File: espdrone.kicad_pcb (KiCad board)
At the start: 6 copper layers, 55 x 55 mm, 565 parts, among them J1 Conn_02x03_Odd_Even, J10 Conn_01x04_Pin, J12 Conn_01x14, J2 Conn_01x02, J3 Conn_Coaxial, J4 Conn_01x04_Pin, J5 Conn_01x04, J6 Conn_01x06, J7 Conn_01x04_Pin, J8 Conn_01x04_Pin, J9 Conn_01x04_Pin, Q1 NMOS, Q10 PSMN1R4-40YLDX, Q11 PSMN1R4-40YLDX, Q12 PSMN1R4-40YLDX, Q13 PSMN1R4-40YLDX, Q14 PSMN1R4-40YLDX, Q15 PSMN1R4-40YLDX, Q16 PSMN1R4-40YLDX, Q17 PSMN1R4-40YLDX, Q18 PSMN1R4-40YLDX, Q19 PSMN1R4-40YLDX, Q2 NMOS, Q20 PSMN1R4-40YLDX, Q21 PSMN1R4-40YLDX, Q22 PSMN1R4-40YLDX, Q23 PSMN1R4-40YLDX, Q24 PSMN1R4-40YLDX, Q25 PSMN1R4-40YLDX, Q26 PSMN1R4-40YLDX, Q27 PSMN1R4-40YLDX, Q28 PSMN1R4-40YLDX, Q3 NMOS, Q4 NMOS, Q5 PSMN1R4-40YLDX, Q6 PSMN1R4-40YLDX, Q7 PSMN1R4-40YLDX, Q8 PSMN1R4-40YLDX, Q9 PSMN1R4-40YLDX, U10 INA180A2, U11 FPC-1.0FX-15PWCR-H20, U12 VL53L1CXV0FY1, U13 LIS2MDL, U14 LSM6DS3, U15 PMW3901MB-TXQT_C43496881, U16 STM32G071K8U6, U17 DRV8328ARUYR, U18 INA180A2, U19 STM32G071K8U6, U2 USBLC6-2P6, U20 DRV8328ARUYR, U21 INA180A2, U22 STM32G071K8U6, U23 DRV8328ARUYR, U24 INA180A2, U25 STM32G071K8U6, U26 DRV8328ARUYR, U27 INA180A2, U3 W25Q128JVP, U4 LFD182G45DCHD277, U5 ESP32-C5HF4, U6 TLV62569DBV, U7 XC6206P182MR_C347373, U8 TPS63070RNMR, U9 TPS2121RUXR, Y1 Crystal_GND24, Y2 Crystal_GND24

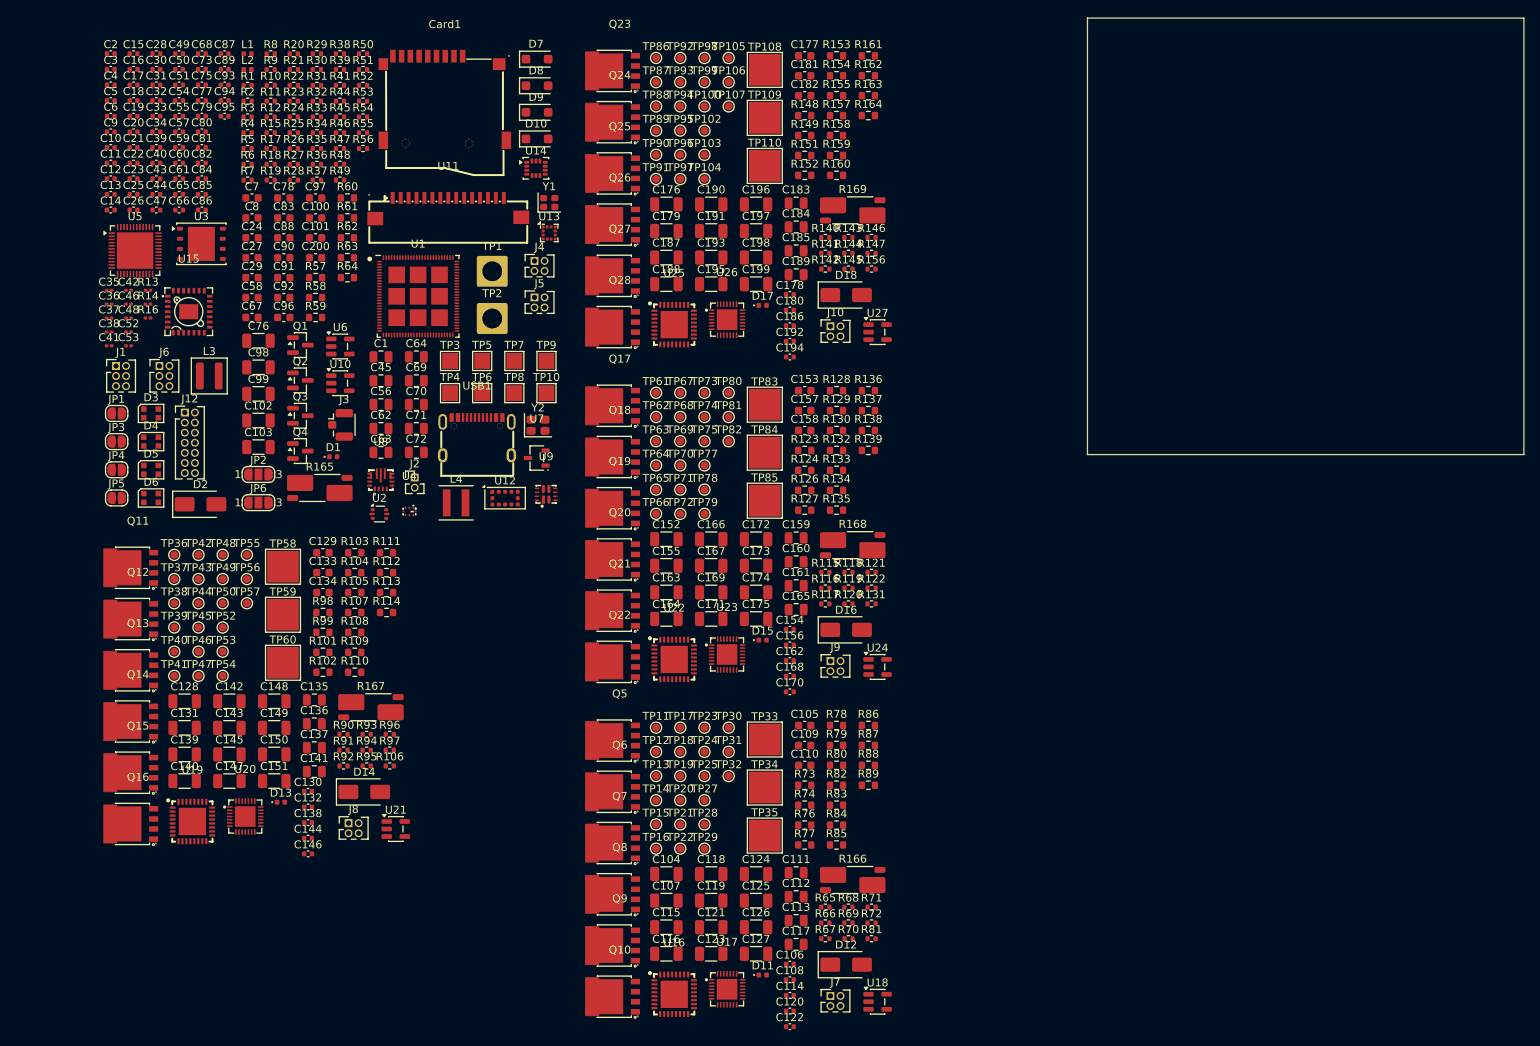
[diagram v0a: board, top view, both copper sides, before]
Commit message: Remove a lot of test points
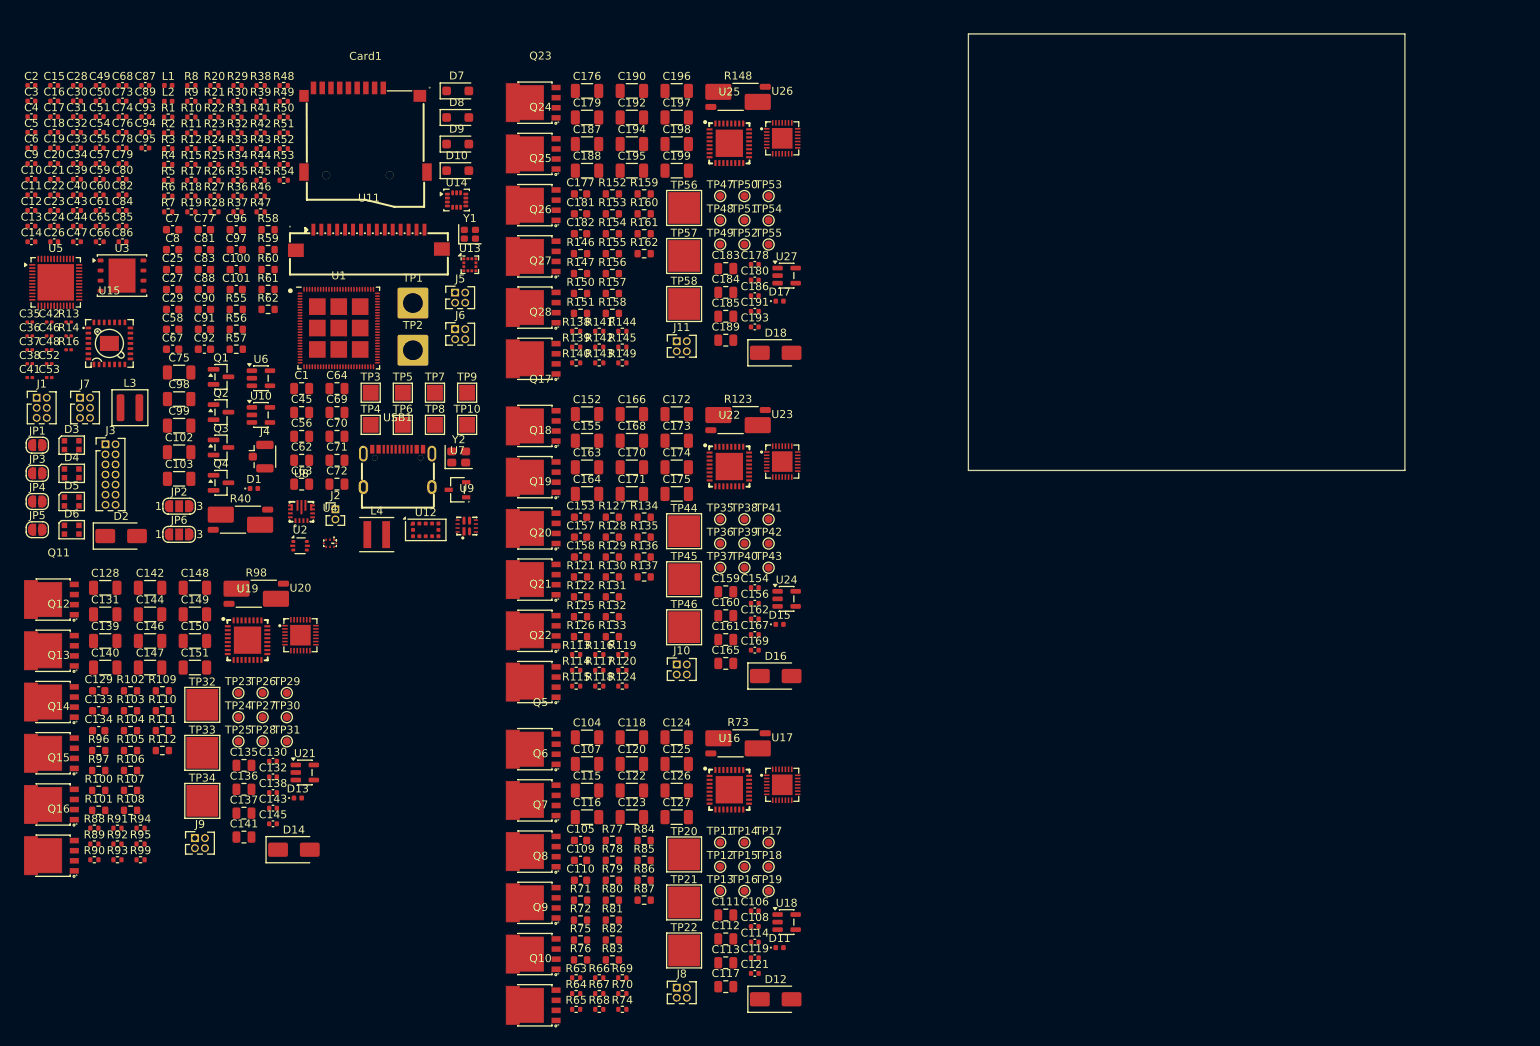
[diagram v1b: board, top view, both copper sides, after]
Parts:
- removed C200: 1u, Capacitor_SMD:C_0603_1608Metric
- removed J12: Conn_01x14, Connector_PinHeader_1.27mm:PinHeader_2x07_P1.27mm_Vertical
- removed R163: 1k, Resistor_SMD:R_0603_1608Metric
- removed R164: 10k, Resistor_SMD:R_0603_1608Metric
- removed R165: 0.0005, Resistor_SMD:R_Shunt_Vishay_WSK2512_6332Metric_T2.66mm
- removed R166, R167, R168, R169: 0.001, Resistor_SMD:R_Shunt_Vishay_WSK2512_6332Metric_T2.66mm
- removed TP100, TP102, TP103, TP104, TP105, TP106, TP107, TP61, TP62, TP63, TP64, TP65, TP66, TP67, TP68, TP69, TP70, TP71, TP72, TP73, TP74, TP75, TP77, TP78, TP79, TP80, TP81, TP82, TP86, TP87, TP88, TP89, TP90, TP91, TP92, TP93, TP94, TP95, TP96, TP97, TP98, TP99: TestPoint, TestPoint:TestPoint_Pad_D1.0mm
- removed TP108, TP83: MOT_A, TestPoint:TestPoint_Pad_4.0x4.0mm
- removed TP109, TP59, TP84: MOT_B, TestPoint:TestPoint_Pad_4.0x4.0mm
- removed TP110, TP60, TP85: MOT_C, TestPoint:TestPoint_Pad_4.0x4.0mm
- added C74: 1n, Capacitor_SMD:C_0402_1005Metric, F.Cu at (65.4, 44.4)
- added J11: Conn_01x04_Pin, Connector_PinHeader_1.27mm:PinHeader_2x02_P1.27mm_Vertical, F.Cu at (135.2, 72.7)
- added R100: 10k, Resistor_SMD:R_0603_1608Metric, F.Cu at (62.4, 129.3)
- added R125: 10k, Resistor_SMD:R_0603_1608Metric, F.Cu at (123.1, 107.4)
- added R150: 10k, Resistor_SMD:R_0603_1608Metric, F.Cu at (123.1, 66.7)
- added R40: 0.0005, Resistor_SMD:R_Shunt_Vishay_WSK2512_6332Metric_T2.66mm, F.Cu at (80.3, 95.2)
- added R42: 47k, Resistor_SMD:R_0402_1005Metric, F.Cu at (82.8, 46.5)
- added R43: 47k, Resistor_SMD:R_0402_1005Metric, F.Cu at (82.8, 48.5)
- added R75: 10k, Resistor_SMD:R_0603_1608Metric, F.Cu at (123.1, 148.2)
- added TP26: TestPoint, TestPoint:TestPoint_Pad_D1.0mm, F.Cu at (83.1, 117.0)
- added TP51: TestPoint, TestPoint:TestPoint_Pad_D1.0mm, F.Cu at (143.8, 57.5)
- C119, C143, C167, C191: value 10u -> 100n; footprint Capacitor_SMD:C_1206_3216Metric -> Capacitor_SMD:C_0402_1005Metric
- C120, C144, C168, C192: value 100n -> 10u; footprint Capacitor_SMD:C_0402_1005Metric -> Capacitor_SMD:C_1206_3216Metric
- C121, C145, C169, C193: value 10u -> 1n; footprint Capacitor_SMD:C_1206_3216Metric -> Capacitor_SMD:C_0402_1005Metric
- C122, C146, C170, C194: value 1n -> 10u; footprint Capacitor_SMD:C_0402_1005Metric -> Capacitor_SMD:C_1206_3216Metric
- C24: value 4.7u -> 100n; footprint Capacitor_SMD:C_0603_1608Metric -> Capacitor_SMD:C_0402_1005Metric
- C25: value 100n -> 4.7u; footprint Capacitor_SMD:C_0402_1005Metric -> Capacitor_SMD:C_0603_1608Metric
- C75: value 1n -> 100u; footprint Capacitor_SMD:C_0402_1005Metric -> Capacitor_SMD:C_1206_3216Metric
- C76: value 100u -> 100n; footprint Capacitor_SMD:C_1206_3216Metric -> Capacitor_SMD:C_0402_1005Metric
- C77: value 100n -> 10u; footprint Capacitor_SMD:C_0402_1005Metric -> Capacitor_SMD:C_0603_1608Metric
- C78: value 10u -> 100n; footprint Capacitor_SMD:C_0603_1608Metric -> Capacitor_SMD:C_0402_1005Metric
- C81: value 100n -> 1u; footprint Capacitor_SMD:C_0402_1005Metric -> Capacitor_SMD:C_0603_1608Metric
- J3: value Conn_Coaxial -> Conn_01x14; footprint Connector_Coaxial:U.FL_Hirose_U.FL-R-SMT-1_Vertical -> Connector_PinHeader_1.27mm:PinHeader_2x07_P1.27mm_Vertical
- J4: value Conn_01x04_Pin -> Conn_Coaxial; footprint Connector_PinHeader_1.27mm:PinHeader_2x02_P1.27mm_Vertical -> Connector_Coaxial:U.FL_Hirose_U.FL-R-SMT-1_Vertical
- J5: value Conn_01x04 -> Conn_01x04_Pin
- J6: value Conn_01x06 -> Conn_01x04; footprint Connector_PinHeader_1.27mm:PinHeader_2x03_P1.27mm_Vertical -> Connector_PinHeader_1.27mm:PinHeader_2x02_P1.27mm_Vertical
- J7: value Conn_01x04_Pin -> Conn_01x06; footprint Connector_PinHeader_1.27mm:PinHeader_2x02_P1.27mm_Vertical -> Connector_PinHeader_1.27mm:PinHeader_2x03_P1.27mm_Vertical
- R101, R120, R126, R145, R151, R70, R76, R95: value 10k -> 1k
- R102, R108, R127, R133, R152, R158, R77, R83: value 1k -> 10
- R104, R110, R129, R135, R154, R160, R57, R58, R61, R62, R79, R85: value 10 -> 10k
- R106, R131, R156, R81: footprint Resistor_SMD:R_0402_1005Metric -> Resistor_SMD:R_0603_1608Metric
- R109, R134, R159, R59, R60, R84: value 10k -> 10
- R111, R136, R161, R86: value 10 -> 1k
- R113, R138, R88: value 1k -> 4.7k; footprint Resistor_SMD:R_0603_1608Metric -> Resistor_SMD:R_0402_1005Metric
- R114, R139, R63, R64, R89: value 10k -> 4.7k; footprint Resistor_SMD:R_0603_1608Metric -> Resistor_SMD:R_0402_1005Metric
- R115, R140, R65, R90: value 4.7k -> 10k
- R116, R141, R66, R91: value 4.7k -> 1k
- R117, R142, R67, R92: value 10k -> 220k
- R118, R143, R68, R93: value 1k -> 10k
- R119, R144, R69, R94: value 220k -> 10k
- R121, R146, R55, R71, R96: value 10k -> 10; footprint Resistor_SMD:R_0402_1005Metric -> Resistor_SMD:R_0603_1608Metric
- R122, R147, R72, R97: value 1k -> 10; footprint Resistor_SMD:R_0402_1005Metric -> Resistor_SMD:R_0603_1608Metric
- R123, R148, R73, R98: value 10 -> 0.001; footprint Resistor_SMD:R_0603_1608Metric -> Resistor_SMD:R_Shunt_Vishay_WSK2512_6332Metric_T2.66mm
- R124, R149, R74, R99: value 10 -> 1k; footprint Resistor_SMD:R_0603_1608Metric -> Resistor_SMD:R_0402_1005Metric
- R34: value 100k -> 10k
- R35: value 10k -> 5k
- R36: value 5k -> 100k
- R47, R48: value 47k -> 10k
- R54: value 10k -> 4.7k
- R56: value 4.7k -> 10; footprint Resistor_SMD:R_0402_1005Metric -> Resistor_SMD:R_0603_1608Metric
- TP20, TP32, TP44, TP56: value TestPoint -> MOT_A; footprint TestPoint:TestPoint_Pad_D1.0mm -> TestPoint:TestPoint_Pad_4.0x4.0mm
- TP21, TP45, TP57: value TestPoint -> MOT_B; footprint TestPoint:TestPoint_Pad_D1.0mm -> TestPoint:TestPoint_Pad_4.0x4.0mm
- TP22, TP46: value TestPoint -> MOT_C; footprint TestPoint:TestPoint_Pad_D1.0mm -> TestPoint:TestPoint_Pad_4.0x4.0mm
- TP33: value MOT_A -> MOT_B
- TP34: value MOT_B -> MOT_C
- TP35: value MOT_C -> TestPoint; footprint TestPoint:TestPoint_Pad_4.0x4.0mm -> TestPoint:TestPoint_Pad_D1.0mm
- TP58: value MOT_A -> MOT_C
- moved J7 120.9 mm to (60.1, 79.8)
- moved R88 97.9 mm to (61.9, 134.1)
- moved R89 97.8 mm to (61.9, 136.1)
- moved R63 95.2 mm to (122.6, 152.9)
- moved R64 94.7 mm to (122.6, 154.9)
- moved TP53 89.6 mm to (146.8, 54.4)
- moved TP54 89.6 mm to (146.8, 57.5)
- moved TP47 89.3 mm to (140.7, 54.4)
- moved TP50 83.4 mm to (143.8, 54.4)
- moved J9 83.1 mm to (74.5, 135.3)
- moved TP52 81.6 mm to (143.8, 60.5)
- moved TP41 77.4 mm to (146.8, 95.2)
- moved TP55 76.5 mm to (146.8, 60.5)
- moved TP48 75.5 mm to (140.7, 57.5)
- moved TP49 75.5 mm to (140.7, 60.5)
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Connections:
- C119 pad 1: GND -> +3V3
- C119 pad 2: +BATT -> GND
- C120 pad 1: +3V3 -> GND
- C120 pad 2: GND -> +BATT
- C121 pad 1: GND -> /Motors/ESC/ISENSE
- C121 pad 2: +BATT -> GND
- C122 pad 1: /Motors/ESC/ISENSE -> GND
- C122 pad 2: GND -> +BATT
- C143 pad 1: GND -> +3V3
- C143 pad 2: +BATT -> GND
- C144 pad 1: +3V3 -> GND
- C144 pad 2: GND -> +BATT
- C145 pad 1: GND -> /Motors/ESC1/ISENSE
- C145 pad 2: +BATT -> GND
- C146 pad 1: /Motors/ESC1/ISENSE -> GND
- C146 pad 2: GND -> +BATT
- C167 pad 1: GND -> +3V3
- C167 pad 2: +BATT -> GND
- C168 pad 1: +3V3 -> GND
- C168 pad 2: GND -> +BATT
- C169 pad 1: GND -> /Motors/ESC2/ISENSE
- C169 pad 2: +BATT -> GND
- C170 pad 1: /Motors/ESC2/ISENSE -> GND
- C170 pad 2: GND -> +BATT
- C191 pad 1: GND -> +3V3
- C191 pad 2: +BATT -> GND
- C192 pad 1: +3V3 -> GND
- C192 pad 2: GND -> +BATT
- C193 pad 1: GND -> /Motors/ESC3/ISENSE
- C193 pad 2: +BATT -> GND
- C194 pad 1: /Motors/ESC3/ISENSE -> GND
- C194 pad 2: GND -> +BATT
- C20 pad 1: +3V3 -> VDD_HP
- C21 pad 1: VDD_HP -> +3V3
- C23 pad 1: VDD_HP -> +3V3
- C24 pad 1: +3V3 -> VDD_HP
- C42 pad 1: Net-(J3-In) -> Net-(J4-In)
- C75 pad 1: BAT_ISENSE -> GND
- C75 pad 2: GND -> Net-(C75-Pad2)
- C76 pad 2: Net-(C76-Pad2) -> +3V3
- C78 pad 1: GND -> +3V3
- C78 pad 2: +3V3 -> GND
- C81 pad 1: +3V3 -> GND
- C81 pad 2: GND -> +3V3
- J10 pad 2: /Motors/ESC3/SWDIO -> /Motors/ESC2/SWDIO
- J10 pad 3: /Motors/ESC3/SWCLK -> /Motors/ESC2/SWCLK
- J3 pad 1: Net-(J3-In) -> +3V3
- J3 pad 2: GND -> /MCU/GPIO6
- J4 pad 1: Net-(J4-Pin_1) -> Net-(J4-In)
- J4 pad 2: Net-(J4-Pin_2) -> GND
- J5 pad 1: +3V3 -> Net-(J5-Pin_1)
- J5 pad 2: I2C_SDA -> Net-(J5-Pin_2)
- J5 pad 3: I2C_SCL -> Net-(J5-Pin_3)
- J5 pad 4: GND -> Net-(J5-Pin_4)
- J6 pad 2: SPI_CLK -> I2C_SDA
- J6 pad 3: SPI_EXT_CS -> I2C_SCL
- J6 pad 4: SPI_MISO -> GND
- J7 pad 2: /Motors/ESC/SWDIO -> SPI_CLK
- J7 pad 3: /Motors/ESC/SWCLK -> SPI_EXT_CS
- J7 pad 4: GND -> SPI_MISO
- J8 pad 2: /Motors/ESC1/SWDIO -> /Motors/ESC/SWDIO
- J8 pad 3: /Motors/ESC1/SWCLK -> /Motors/ESC/SWCLK
- J9 pad 2: /Motors/ESC2/SWDIO -> /Motors/ESC1/SWDIO
- J9 pad 3: /Motors/ESC2/SWCLK -> /Motors/ESC1/SWCLK
- JP2 pad 2: Net-(J4-Pin_2) -> Net-(J5-Pin_2)
- R101 pad 1: /Motors/ESC1/VSENSE_A -> GND
- R101 pad 2: /Motors/ESC1/VSENSE_REF -> /Motors/ESC1/VSENSE_A
- R102 pad 1: GND -> Net-(Q13-G)
- R102 pad 2: /Motors/ESC1/VSENSE_A -> /Motors/ESC1/GHB
- R103 pad 1: Net-(Q13-G) -> Net-(Q14-G)
- R103 pad 2: /Motors/ESC1/GHB -> /Motors/ESC1/GLB
- R104 pad 1: Net-(Q14-G) -> /Motors/ESC1/A
- R104 pad 2: /Motors/ESC1/GLB -> /Motors/ESC1/VSENSE_A
- R105 pad 1: /Motors/ESC1/A -> /Motors/ESC1/VSENSE_B
- R105 pad 2: /Motors/ESC1/VSENSE_A -> /Motors/ESC1/VSENSE_REF
- R106 pad 1: /Motors/ESC1/ISENSE -> GND
- R106 pad 2: Net-(R106-Pad2) -> /Motors/ESC1/VSENSE_B
- R107 pad 1: /Motors/ESC1/VSENSE_B -> /Motors/ESC1/B
- R107 pad 2: /Motors/ESC1/VSENSE_REF -> /Motors/ESC1/VSENSE_B
- R108 pad 1: GND -> Net-(Q15-G)
- R108 pad 2: /Motors/ESC1/VSENSE_B -> /Motors/ESC1/GHC
- R109 pad 1: /Motors/ESC1/B -> Net-(Q16-G)
- R109 pad 2: /Motors/ESC1/VSENSE_B -> /Motors/ESC1/GLC
- R110 pad 1: Net-(Q15-G) -> /Motors/ESC1/VSENSE_C
- R110 pad 2: /Motors/ESC1/GHC -> /Motors/ESC1/VSENSE_REF
- R111 pad 1: Net-(Q16-G) -> GND
- R111 pad 2: /Motors/ESC1/GLC -> /Motors/ESC1/VSENSE_C
- R112 pad 1: /Motors/ESC1/VSENSE_C -> /Motors/ESC1/C
- R112 pad 2: /Motors/ESC1/VSENSE_REF -> /Motors/ESC1/VSENSE_C
- R113 pad 1: GND -> Net-(U22-PA0)
- R113 pad 2: /Motors/ESC1/VSENSE_C -> Net-(D15-A)
- R114 pad 1: /Motors/ESC1/C -> +3V3
- R114 pad 2: /Motors/ESC1/VSENSE_C -> /Motors/ESC2/NFAULT
- R115 pad 1: Net-(U22-PA0) -> Net-(U23-DT)
- R115 pad 2: Net-(D15-A) -> GND
- R116 pad 1: +3V3 -> Net-(U22-PB4)
- R116 pad 2: /Motors/ESC2/NFAULT -> DSHOT_3
- R117 pad 1: Net-(U23-DT) -> Net-(U23-VDSLVL)
- R117 pad 2: GND -> +3V3
- R118 pad 1: Net-(U22-PB4) -> GND
- R118 pad 2: DSHOT_3 -> Net-(U23-VDSLVL)
- R119 pad 1: Net-(U23-VDSLVL) -> /Motors/ESC2/VSENSE
- R119 pad 2: +3V3 -> +BATT
- R120 pad 2: Net-(U23-VDSLVL) -> /Motors/ESC2/VSENSE
- R121 pad 1: /Motors/ESC2/VSENSE -> Net-(Q17-G)
- R121 pad 2: +BATT -> /Motors/ESC2/GHA
- R122 pad 1: GND -> Net-(Q18-G)
- R122 pad 2: /Motors/ESC2/VSENSE -> /Motors/ESC2/GLA
- R123 pad 1: Net-(Q17-G) -> GND
- R123 pad 2: /Motors/ESC2/GHA -> Net-(U24--)
- R124 pad 1: Net-(Q18-G) -> /Motors/ESC2/ISENSE
- R124 pad 2: /Motors/ESC2/GLA -> Net-(R124-Pad2)
- R126 pad 1: /Motors/ESC2/VSENSE_A -> GND
- R126 pad 2: /Motors/ESC2/VSENSE_REF -> /Motors/ESC2/VSENSE_A
- R127 pad 1: GND -> Net-(Q19-G)
- R127 pad 2: /Motors/ESC2/VSENSE_A -> /Motors/ESC2/GHB
- R128 pad 1: Net-(Q19-G) -> Net-(Q20-G)
- R128 pad 2: /Motors/ESC2/GHB -> /Motors/ESC2/GLB
- R129 pad 1: Net-(Q20-G) -> /Motors/ESC2/A
- R129 pad 2: /Motors/ESC2/GLB -> /Motors/ESC2/VSENSE_A
- R130 pad 1: /Motors/ESC2/A -> /Motors/ESC2/VSENSE_B
- R130 pad 2: /Motors/ESC2/VSENSE_A -> /Motors/ESC2/VSENSE_REF
- R131 pad 1: /Motors/ESC2/ISENSE -> GND
- R131 pad 2: Net-(R131-Pad2) -> /Motors/ESC2/VSENSE_B
- R132 pad 1: /Motors/ESC2/VSENSE_B -> /Motors/ESC2/B
- R132 pad 2: /Motors/ESC2/VSENSE_REF -> /Motors/ESC2/VSENSE_B
- R133 pad 1: GND -> Net-(Q21-G)
- R133 pad 2: /Motors/ESC2/VSENSE_B -> /Motors/ESC2/GHC
- R134 pad 1: /Motors/ESC2/B -> Net-(Q22-G)
- R134 pad 2: /Motors/ESC2/VSENSE_B -> /Motors/ESC2/GLC
- R135 pad 1: Net-(Q21-G) -> /Motors/ESC2/VSENSE_C
- R135 pad 2: /Motors/ESC2/GHC -> /Motors/ESC2/VSENSE_REF
- R136 pad 1: Net-(Q22-G) -> GND
- R136 pad 2: /Motors/ESC2/GLC -> /Motors/ESC2/VSENSE_C
- R137 pad 1: /Motors/ESC2/VSENSE_C -> /Motors/ESC2/C
- R137 pad 2: /Motors/ESC2/VSENSE_REF -> /Motors/ESC2/VSENSE_C
- R138 pad 1: GND -> Net-(U25-PA0)
- R138 pad 2: /Motors/ESC2/VSENSE_C -> Net-(D17-A)
- R139 pad 1: /Motors/ESC2/C -> +3V3
- R139 pad 2: /Motors/ESC2/VSENSE_C -> /Motors/ESC3/NFAULT
- R140 pad 1: Net-(U25-PA0) -> Net-(U26-DT)
- R140 pad 2: Net-(D17-A) -> GND
- R141 pad 1: +3V3 -> Net-(U25-PB4)
- R141 pad 2: /Motors/ESC3/NFAULT -> DSHOT_4
- R142 pad 1: Net-(U26-DT) -> Net-(U26-VDSLVL)
- R142 pad 2: GND -> +3V3
- R143 pad 1: Net-(U25-PB4) -> GND
- R143 pad 2: DSHOT_4 -> Net-(U26-VDSLVL)
- R144 pad 1: Net-(U26-VDSLVL) -> /Motors/ESC3/VSENSE
- R144 pad 2: +3V3 -> +BATT
- R145 pad 2: Net-(U26-VDSLVL) -> /Motors/ESC3/VSENSE
- R146 pad 1: /Motors/ESC3/VSENSE -> Net-(Q23-G)
- R146 pad 2: +BATT -> /Motors/ESC3/GHA
- R147 pad 1: GND -> Net-(Q24-G)
- R147 pad 2: /Motors/ESC3/VSENSE -> /Motors/ESC3/GLA
- R148 pad 1: Net-(Q23-G) -> GND
- R148 pad 2: /Motors/ESC3/GHA -> Net-(U27--)
- R149 pad 1: Net-(Q24-G) -> /Motors/ESC3/ISENSE
- R149 pad 2: /Motors/ESC3/GLA -> Net-(R149-Pad2)
- R151 pad 1: /Motors/ESC3/VSENSE_A -> GND
- R151 pad 2: /Motors/ESC3/VSENSE_REF -> /Motors/ESC3/VSENSE_A
- R152 pad 1: GND -> Net-(Q25-G)
- R152 pad 2: /Motors/ESC3/VSENSE_A -> /Motors/ESC3/GHB
- R153 pad 1: Net-(Q25-G) -> Net-(Q26-G)
- R153 pad 2: /Motors/ESC3/GHB -> /Motors/ESC3/GLB
- R154 pad 1: Net-(Q26-G) -> /Motors/ESC3/A
- R154 pad 2: /Motors/ESC3/GLB -> /Motors/ESC3/VSENSE_A
- R155 pad 1: /Motors/ESC3/A -> /Motors/ESC3/VSENSE_B
- R155 pad 2: /Motors/ESC3/VSENSE_A -> /Motors/ESC3/VSENSE_REF
- R156 pad 1: /Motors/ESC3/ISENSE -> GND
- R156 pad 2: Net-(R156-Pad2) -> /Motors/ESC3/VSENSE_B
- R157 pad 1: /Motors/ESC3/VSENSE_B -> /Motors/ESC3/B
- R157 pad 2: /Motors/ESC3/VSENSE_REF -> /Motors/ESC3/VSENSE_B
- R158 pad 1: GND -> Net-(Q27-G)
- R158 pad 2: /Motors/ESC3/VSENSE_B -> /Motors/ESC3/GHC
- R159 pad 1: /Motors/ESC3/B -> Net-(Q28-G)
- R159 pad 2: /Motors/ESC3/VSENSE_B -> /Motors/ESC3/GLC
- R16 pad 1: Net-(J3-In) -> Net-(J4-In)
- R160 pad 1: Net-(Q27-G) -> /Motors/ESC3/VSENSE_C
- R160 pad 2: /Motors/ESC3/GHC -> /Motors/ESC3/VSENSE_REF
- R161 pad 1: Net-(Q28-G) -> GND
- R161 pad 2: /Motors/ESC3/GLC -> /Motors/ESC3/VSENSE_C
- R162 pad 1: /Motors/ESC3/VSENSE_C -> /Motors/ESC3/C
- R162 pad 2: /Motors/ESC3/VSENSE_REF -> /Motors/ESC3/VSENSE_C
- R34 pad 1: +3V3 -> +5V
- R34 pad 2: Net-(U8-PG) -> Net-(U9-PR1)
- R35 pad 1: +5V -> Net-(U9-PR1)
- R35 pad 2: Net-(U9-PR1) -> GND
- R36 pad 1: Net-(U9-PR1) -> +3V3
- R36 pad 2: GND -> Net-(U8-PG)
- R44 pad 1: SD_SDIO_D2 -> SD_SDIO_CMD
- R45 pad 1: SD_SDIO_D3 -> SD_SDIO_D0
- R46 pad 1: SD_SDIO_CMD -> SD_SDIO_D1
- R47 pad 1: SD_SDIO_D0 -> Net-(U12-XSHUT)
- R48 pad 1: SD_SDIO_D1 -> Net-(U13-~{CS})
- R49 pad 1: Net-(U12-XSHUT) -> Net-(U14-CS)
- R50 pad 1: Net-(U13-~{CS}) -> Net-(U15-NRESET)
- R51 pad 1: Net-(U14-CS) -> I2C_SDA
- R52 pad 1: Net-(U15-NRESET) -> SPI_PMW3901_CS
- R53 pad 1: I2C_SDA -> I2C_SCL
- R54 pad 1: SPI_PMW3901_CS -> +3V3
- R54 pad 2: +3V3 -> SPI_EXT_CS
- R55 pad 1: I2C_SCL -> DC_MOT1
- R55 pad 2: +3V3 -> Net-(Q1-G)
- R56 pad 1: +3V3 -> DC_MOT3
- R56 pad 2: SPI_EXT_CS -> Net-(Q2-G)
- R57 pad 1: DC_MOT1 -> Net-(Q1-G)
- R57 pad 2: Net-(Q1-G) -> GND
- R58 pad 1: DC_MOT3 -> Net-(Q2-G)
- R58 pad 2: Net-(Q2-G) -> GND
- R59 pad 1: Net-(Q1-G) -> DC_MOT2
- R59 pad 2: GND -> Net-(Q3-G)
- R6 pad 1: Net-(JP1-B) -> Net-(U1-GPIO36)
- R6 pad 2: GND -> +3V3
- R60 pad 1: Net-(Q2-G) -> DC_MOT4
- R60 pad 2: GND -> Net-(Q4-G)
- R61 pad 1: DC_MOT2 -> Net-(Q3-G)
- R61 pad 2: Net-(Q3-G) -> GND
- R62 pad 1: DC_MOT4 -> Net-(Q4-G)
- R62 pad 2: Net-(Q4-G) -> GND
- R63 pad 1: Net-(Q3-G) -> Net-(U16-PA0)
- R63 pad 2: GND -> Net-(D11-A)
- R64 pad 1: Net-(Q4-G) -> +3V3
- R64 pad 2: GND -> /Motors/ESC/NFAULT
- R65 pad 1: Net-(U16-PA0) -> Net-(U17-DT)
- R65 pad 2: Net-(D11-A) -> GND
- R66 pad 1: +3V3 -> Net-(U16-PB4)
- R66 pad 2: /Motors/ESC/NFAULT -> DSHOT_1
- R67 pad 1: Net-(U17-DT) -> Net-(U17-VDSLVL)
- R67 pad 2: GND -> +3V3
- R68 pad 1: Net-(U16-PB4) -> GND
- R68 pad 2: DSHOT_1 -> Net-(U17-VDSLVL)
- R69 pad 1: Net-(U17-VDSLVL) -> /Motors/ESC/VSENSE
- R69 pad 2: +3V3 -> +BATT
- R7 pad 1: Net-(U1-GPIO36) -> Net-(JP1-B)
- R7 pad 2: +3V3 -> GND
- R70 pad 2: Net-(U17-VDSLVL) -> /Motors/ESC/VSENSE
- R71 pad 1: /Motors/ESC/VSENSE -> Net-(Q5-G)
- R71 pad 2: +BATT -> /Motors/ESC/GHA
- R72 pad 1: GND -> Net-(Q6-G)
- R72 pad 2: /Motors/ESC/VSENSE -> /Motors/ESC/GLA
- R73 pad 1: Net-(Q5-G) -> GND
- R73 pad 2: /Motors/ESC/GHA -> Net-(U18--)
- R74 pad 1: Net-(Q6-G) -> /Motors/ESC/ISENSE
- R74 pad 2: /Motors/ESC/GLA -> Net-(R74-Pad2)
- R76 pad 1: /Motors/ESC/VSENSE_A -> GND
- R76 pad 2: /Motors/ESC/VSENSE_REF -> /Motors/ESC/VSENSE_A
- R77 pad 1: GND -> Net-(Q7-G)
- R77 pad 2: /Motors/ESC/VSENSE_A -> /Motors/ESC/GHB
- R78 pad 1: Net-(Q7-G) -> Net-(Q8-G)
- R78 pad 2: /Motors/ESC/GHB -> /Motors/ESC/GLB
- R79 pad 1: Net-(Q8-G) -> /Motors/ESC/A
- R79 pad 2: /Motors/ESC/GLB -> /Motors/ESC/VSENSE_A
- R80 pad 1: /Motors/ESC/A -> /Motors/ESC/VSENSE_B
- R80 pad 2: /Motors/ESC/VSENSE_A -> /Motors/ESC/VSENSE_REF
- R81 pad 1: /Motors/ESC/ISENSE -> GND
- R81 pad 2: Net-(R81-Pad2) -> /Motors/ESC/VSENSE_B
- R82 pad 1: /Motors/ESC/VSENSE_B -> /Motors/ESC/B
- R82 pad 2: /Motors/ESC/VSENSE_REF -> /Motors/ESC/VSENSE_B
- R83 pad 1: GND -> Net-(Q9-G)
- R83 pad 2: /Motors/ESC/VSENSE_B -> /Motors/ESC/GHC
- R84 pad 1: /Motors/ESC/B -> Net-(Q10-G)
- R84 pad 2: /Motors/ESC/VSENSE_B -> /Motors/ESC/GLC
- R85 pad 1: Net-(Q9-G) -> /Motors/ESC/VSENSE_C
- R85 pad 2: /Motors/ESC/GHC -> /Motors/ESC/VSENSE_REF
- R86 pad 1: Net-(Q10-G) -> GND
- R86 pad 2: /Motors/ESC/GLC -> /Motors/ESC/VSENSE_C
- R87 pad 1: /Motors/ESC/VSENSE_C -> /Motors/ESC/C
- R87 pad 2: /Motors/ESC/VSENSE_REF -> /Motors/ESC/VSENSE_C
- R88 pad 1: GND -> Net-(U19-PA0)
- R88 pad 2: /Motors/ESC/VSENSE_C -> Net-(D13-A)
- R89 pad 1: /Motors/ESC/C -> +3V3
- R89 pad 2: /Motors/ESC/VSENSE_C -> /Motors/ESC1/NFAULT
- R90 pad 1: Net-(U19-PA0) -> Net-(U20-DT)
- R90 pad 2: Net-(D13-A) -> GND
- R91 pad 1: +3V3 -> Net-(U19-PB4)
- R91 pad 2: /Motors/ESC1/NFAULT -> DSHOT_2
- R92 pad 1: Net-(U20-DT) -> Net-(U20-VDSLVL)
- R92 pad 2: GND -> +3V3
- R93 pad 1: Net-(U19-PB4) -> GND
- R93 pad 2: DSHOT_2 -> Net-(U20-VDSLVL)
- R94 pad 1: Net-(U20-VDSLVL) -> /Motors/ESC1/VSENSE
- R94 pad 2: +3V3 -> +BATT
- R95 pad 2: Net-(U20-VDSLVL) -> /Motors/ESC1/VSENSE
- R96 pad 1: /Motors/ESC1/VSENSE -> Net-(Q11-G)
- R96 pad 2: +BATT -> /Motors/ESC1/GHA
- R97 pad 1: GND -> Net-(Q12-G)
- R97 pad 2: /Motors/ESC1/VSENSE -> /Motors/ESC1/GLA
- R98 pad 1: Net-(Q11-G) -> GND
- R98 pad 2: /Motors/ESC1/GHA -> Net-(U21--)
- R99 pad 1: Net-(Q12-G) -> /Motors/ESC1/ISENSE
- R99 pad 2: /Motors/ESC1/GLA -> Net-(R99-Pad2)
- TP1 pad 1: Net-(C76-Pad2) -> Net-(C75-Pad2)
- TP17 pad 1: /Motors/ESC/VSENSE_A -> /Motors/ESC/NRST
- TP18 pad 1: /Motors/ESC/VSENSE_B -> /Motors/ESC/NSLEEP
- TP19 pad 1: /Motors/ESC/VSENSE_C -> /Motors/ESC/TELEMETRY
- TP20 pad 1: /Motors/ESC/VSENSE_REF -> /Motors/ESC/A
- TP21 pad 1: /Motors/ESC/ISENSE -> /Motors/ESC/B
- TP22 pad 1: /Motors/ESC/LSS -> /Motors/ESC/C
- TP23 pad 1: DSHOT_1 -> /Motors/ESC1/A_LOW
- TP24 pad 1: /Motors/ESC/TELEMETRY -> /Motors/ESC1/B_LOW
- TP25 pad 1: /Motors/ESC/GVDD -> /Motors/ESC1/C_LOW
- TP27 pad 1: /Motors/ESC/BSTA -> /Motors/ESC1/B_HIGH
- TP28 pad 1: /Motors/ESC/VSENSE -> /Motors/ESC1/C_HIGH
- TP29 pad 1: /Motors/ESC/NRST -> /Motors/ESC1/NRST
- TP30 pad 1: /Motors/ESC/NSLEEP -> /Motors/ESC1/NSLEEP
- TP31 pad 1: +BATT -> /Motors/ESC1/TELEMETRY
- TP32 pad 1: GND -> /Motors/ESC1/A
- TP33 pad 1: /Motors/ESC/A -> /Motors/ESC1/B
- TP34 pad 1: /Motors/ESC/B -> /Motors/ESC1/C
- TP35 pad 1: /Motors/ESC/C -> /Motors/ESC2/A_LOW
- TP36 pad 1: /Motors/ESC1/A_LOW -> /Motors/ESC2/B_LOW
- TP37 pad 1: /Motors/ESC1/B_LOW -> /Motors/ESC2/C_LOW
- TP38 pad 1: /Motors/ESC1/C_LOW -> /Motors/ESC2/A_HIGH
- TP39 pad 1: /Motors/ESC1/A_HIGH -> /Motors/ESC2/B_HIGH
- TP40 pad 1: /Motors/ESC1/B_HIGH -> /Motors/ESC2/C_HIGH
- TP41 pad 1: /Motors/ESC1/C_HIGH -> /Motors/ESC2/NRST
- TP42 pad 1: /Motors/ESC1/VSENSE_A -> /Motors/ESC2/NSLEEP
- TP43 pad 1: /Motors/ESC1/VSENSE_B -> /Motors/ESC2/TELEMETRY
- TP44 pad 1: /Motors/ESC1/VSENSE_C -> /Motors/ESC2/A
- TP45 pad 1: /Motors/ESC1/VSENSE_REF -> /Motors/ESC2/B
- TP46 pad 1: /Motors/ESC1/ISENSE -> /Motors/ESC2/C
- TP47 pad 1: /Motors/ESC1/LSS -> /Motors/ESC3/A_LOW
- TP48 pad 1: DSHOT_2 -> /Motors/ESC3/B_LOW
- TP49 pad 1: /Motors/ESC1/TELEMETRY -> /Motors/ESC3/C_LOW
- TP50 pad 1: /Motors/ESC1/GVDD -> /Motors/ESC3/A_HIGH
- TP52 pad 1: /Motors/ESC1/BSTA -> /Motors/ESC3/C_HIGH
- TP53 pad 1: /Motors/ESC1/VSENSE -> /Motors/ESC3/NRST
- TP54 pad 1: /Motors/ESC1/NRST -> /Motors/ESC3/NSLEEP
- TP55 pad 1: /Motors/ESC1/NSLEEP -> /Motors/ESC3/TELEMETRY
- TP56 pad 1: +BATT -> /Motors/ESC3/A
- TP57 pad 1: GND -> /Motors/ESC3/B
- TP58 pad 1: /Motors/ESC1/A -> /Motors/ESC3/C
- U18 pad 1: Net-(R81-Pad2) -> Net-(R74-Pad2)
- U21 pad 1: Net-(R106-Pad2) -> Net-(R99-Pad2)
- U24 pad 1: Net-(R131-Pad2) -> Net-(R124-Pad2)
- U27 pad 1: Net-(R156-Pad2) -> Net-(R149-Pad2)
- U5 pad 11: Net-(J4-Pin_1) -> Net-(J5-Pin_1)
- U5 pad 12: Net-(J4-Pin_2) -> Net-(J5-Pin_2)
- U5 pad 13: Net-(J4-Pin_3) -> Net-(J5-Pin_3)
- U5 pad 14: Net-(J4-Pin_4) -> Net-(J5-Pin_4)
